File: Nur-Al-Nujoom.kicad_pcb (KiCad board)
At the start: 2 copper layers, 1 part, among them U1 STM32F030C8T6TR

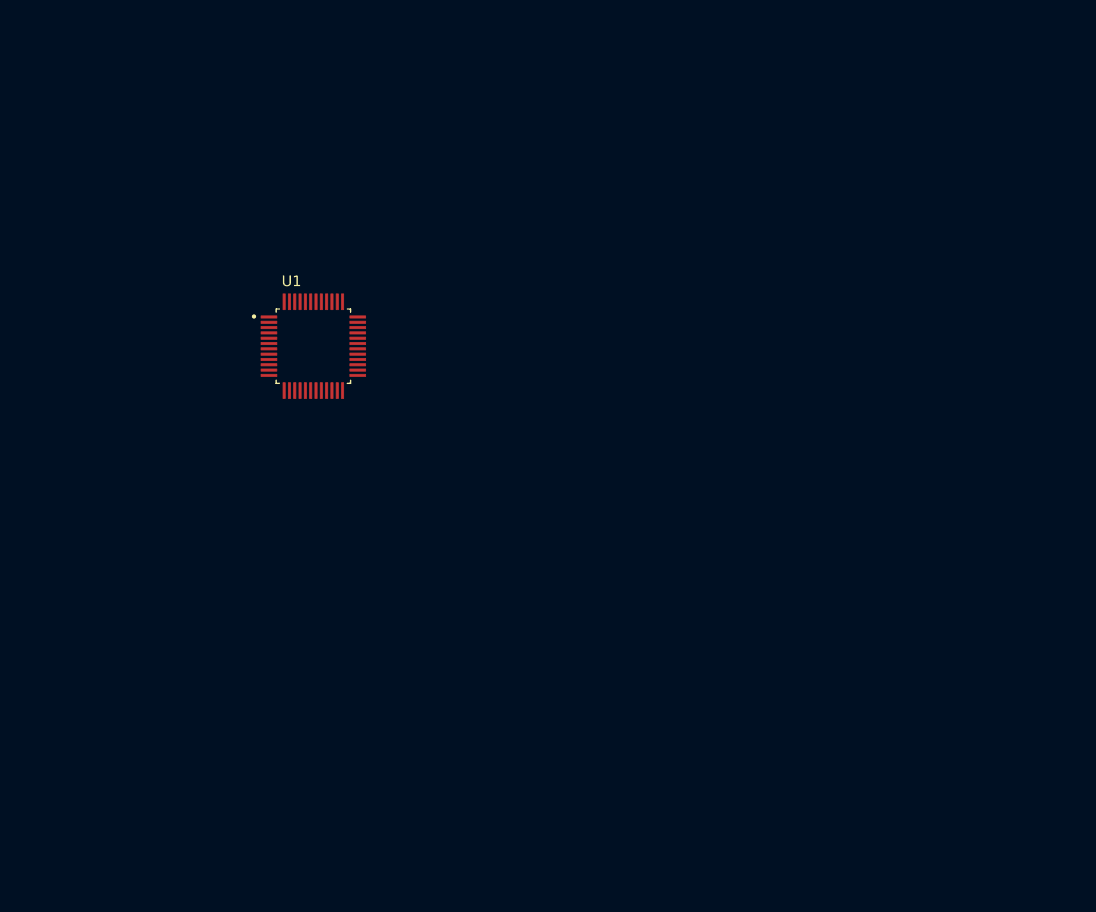
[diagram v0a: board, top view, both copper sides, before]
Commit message: updated Routing
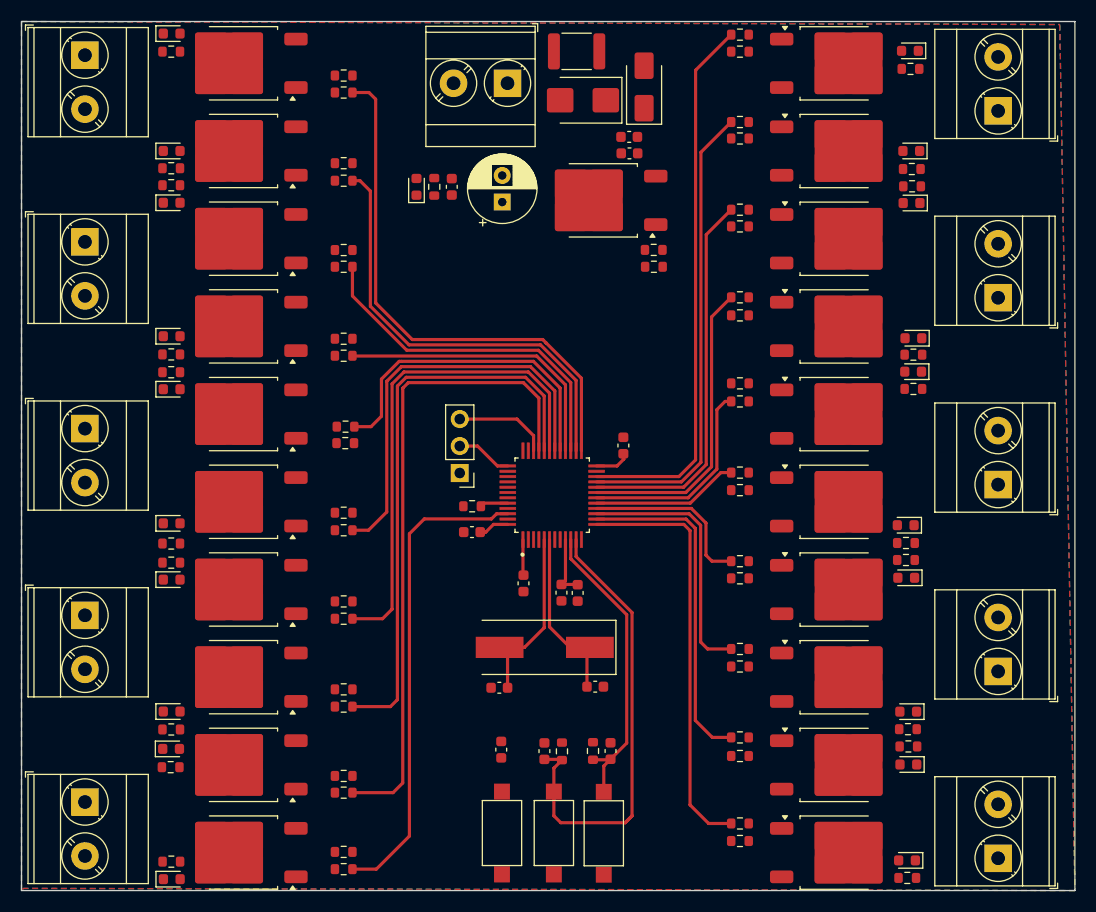
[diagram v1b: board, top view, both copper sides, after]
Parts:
- added C1: 10uF, Capacitor_SMD:C_0603_1608Metric, F.Cu at (172.7, 63.0)
- added C10: 100nF, Capacitor_SMD:C_0603_1608Metric, F.Cu at (160.7, 119.1)
- added C11: 20pF, Capacitor_SMD:C_0603_1608Metric, F.Cu at (169.5, 113.2)
- added C12: 20pF, Capacitor_SMD:C_0603_1608Metric, F.Cu at (160.5, 113.3)
- added C13: 100nF, Capacitor_SMD:C_0603_1608Metric, F.Cu at (170.9, 119.3)
- added C14: 100nF, Capacitor_SMD:C_0603_1608Metric, F.Cu at (164.7, 119.3)
- added C2: 100nF, Capacitor_SMD:C_0603_1608Metric, F.Cu at (172.7, 61.5)
- added C3: 100uF, Capacitor_THT:CP_Radial_D6.3mm_P2.50mm, F.Cu at (160.8, 67.6)
- added C4: 100nF, Capacitor_SMD:C_0603_1608Metric, F.Cu at (156.0, 66.2)
- added C5: 4.7uF, Capacitor_SMD:C_0603_1608Metric, F.Cu at (172.2, 90.5)
- added C6: 100nF, Capacitor_SMD:C_0603_1608Metric, F.Cu at (157.9, 98.7)
- added C7: 100nF, Capacitor_SMD:C_0603_1608Metric, F.Cu at (162.8, 103.5)
- added C8: 1uF, Capacitor_SMD:C_0603_1608Metric, F.Cu at (166.3, 104.3)
- added C9: 10nF, Capacitor_SMD:C_0603_1608Metric, F.Cu at (167.8, 104.4)
- added D1: SMBJ18CA, Diode_SMD:D_SMB, F.Cu at (168.3, 58.0)
- added D10: LED_Small, LED_SMD:LED_0603_1608Metric, F.Cu at (199.4, 83.5)
- added D11: LED_Small, LED_SMD:LED_0603_1608Metric, F.Cu at (199.2, 62.8)
- added D12: LED_Small, LED_SMD:LED_0603_1608Metric, F.Cu at (199.1, 53.4)
- added D13: LED_Small, LED_SMD:LED_0603_1608Metric, F.Cu at (199.4, 80.4)
- added D14: LED_Small, LED_SMD:LED_0603_1608Metric, F.Cu at (129.6, 115.5)
- added D15: LED_Small, LED_SMD:LED_0603_1608Metric, F.Cu at (129.6, 131.3)
- added D16: LED_Small, LED_SMD:LED_0603_1608Metric, F.Cu at (129.6, 103.1)
- added D17: LED_Small, LED_SMD:LED_0603_1608Metric, F.Cu at (129.6, 97.8)
- added D18: LED_Small, LED_SMD:LED_0603_1608Metric, F.Cu at (129.6, 119.1)
- added D19: LED_Small, LED_SMD:LED_0603_1608Metric, F.Cu at (129.6, 67.7)
- added D2: SS34, Diode_SMD:D_SMA, F.Cu at (174.1, 56.8)
- added D20: LED_Small, LED_SMD:LED_0603_1608Metric, F.Cu at (129.6, 85.2)
- added D21: LED_Small, LED_SMD:LED_0603_1608Metric, F.Cu at (129.6, 62.8)
- added D22: LED_Small, LED_SMD:LED_0603_1608Metric, F.Cu at (129.6, 51.7)
- added D23: LED_Small, LED_SMD:LED_0603_1608Metric, F.Cu at (129.6, 80.2)
- added D3: LED, LED_SMD:LED_0603_1608Metric, F.Cu at (152.7, 66.2)
- added D4: LED_Small, LED_SMD:LED_0603_1608Metric, F.Cu at (198.8, 129.6)
- added D5: LED_Small, LED_SMD:LED_0603_1608Metric, F.Cu at (199.0, 120.5)
- added D6: LED_Small, LED_SMD:LED_0603_1608Metric, F.Cu at (199.0, 115.5)
- added D7: LED_Small, LED_SMD:LED_0603_1608Metric, F.Cu at (198.8, 103.0)
- added D8: LED_Small, LED_SMD:LED_0603_1608Metric, F.Cu at (198.7, 98.0)
- added D9: LED_Small, LED_SMD:LED_0603_1608Metric, F.Cu at (199.3, 67.7)
- added J1: Main_12+, TerminalBlock_Phoenix:TerminalBlock_Phoenix_MKDS-3-2-5.08_1x02_P5.08mm_Horizontal, F.Cu at (161.2, 56.4)
- added J10: C1,2, TerminalBlock_Phoenix:TerminalBlock_Phoenix_MKDS-3-2-5.08_1x02_P5.08mm_Horizontal, F.Cu at (121.5, 88.9)
- added J11: C1,2, TerminalBlock_Phoenix:TerminalBlock_Phoenix_MKDS-3-2-5.08_1x02_P5.08mm_Horizontal, F.Cu at (121.5, 71.3)
- added J12: C1,2, TerminalBlock_Phoenix:TerminalBlock_Phoenix_MKDS-3-2-5.08_1x02_P5.08mm_Horizontal, F.Cu at (121.5, 53.8)
- added J2: SWD, Connector_PinHeader_2.54mm:PinHeader_1x03_P2.54mm_Vertical, F.Cu at (156.8, 93.1)
- added J3: C1,2, TerminalBlock_Phoenix:TerminalBlock_Phoenix_MKDS-3-2-5.08_1x02_P5.08mm_Horizontal, F.Cu at (207.4, 129.3)
- added J4: C1,2, TerminalBlock_Phoenix:TerminalBlock_Phoenix_MKDS-3-2-5.08_1x02_P5.08mm_Horizontal, F.Cu at (207.4, 111.8)
- added J5: C1,2, TerminalBlock_Phoenix:TerminalBlock_Phoenix_MKDS-3-2-5.08_1x02_P5.08mm_Horizontal, F.Cu at (207.4, 94.2)
- added J6: C1,2, TerminalBlock_Phoenix:TerminalBlock_Phoenix_MKDS-3-2-5.08_1x02_P5.08mm_Horizontal, F.Cu at (207.4, 76.6)
- added J7: C1,2, TerminalBlock_Phoenix:TerminalBlock_Phoenix_MKDS-3-2-5.08_1x02_P5.08mm_Horizontal, F.Cu at (207.4, 59.0)
- added J8: C1,2, TerminalBlock_Phoenix:TerminalBlock_Phoenix_MKDS-3-2-5.08_1x02_P5.08mm_Horizontal, F.Cu at (121.5, 124.1)
- added J9: C1,2, TerminalBlock_Phoenix:TerminalBlock_Phoenix_MKDS-3-2-5.08_1x02_P5.08mm_Horizontal, F.Cu at (121.5, 106.5)
- added Q1: MOT90N03D, Package_TO_SOT_SMD:TO-252-2, F.Cu at (192.1, 128.8)
- added Q10: MOT90N03D, Package_TO_SOT_SMD:TO-252-2, F.Cu at (192.1, 79.3)
- added Q11: MOT90N03D, Package_TO_SOT_SMD:TO-252-2, F.Cu at (136.3, 112.3)
- added Q12: MOT90N03D, Package_TO_SOT_SMD:TO-252-2, F.Cu at (136.3, 128.8)
- added Q13: MOT90N03D, Package_TO_SOT_SMD:TO-252-2, F.Cu at (136.3, 104.1)
- added Q14: MOT90N03D, Package_TO_SOT_SMD:TO-252-2, F.Cu at (136.3, 95.8)
- added Q15: MOT90N03D, Package_TO_SOT_SMD:TO-252-2, F.Cu at (136.3, 120.6)
- added Q16: MOT90N03D, Package_TO_SOT_SMD:TO-252-2, F.Cu at (136.3, 71.0)
- added Q17: MOT90N03D, Package_TO_SOT_SMD:TO-252-2, F.Cu at (136.3, 87.5)
- added Q18: MOT90N03D, Package_TO_SOT_SMD:TO-252-2, F.Cu at (136.3, 62.8)
- added Q19: MOT90N03D, Package_TO_SOT_SMD:TO-252-2, F.Cu at (136.3, 54.5)
- added Q2: MOT90N03D, Package_TO_SOT_SMD:TO-252-2, F.Cu at (192.1, 120.6)
- added Q20: MOT90N03D, Package_TO_SOT_SMD:TO-252-2, F.Cu at (136.3, 79.3)
- added Q3: MOT90N03D, Package_TO_SOT_SMD:TO-252-2, F.Cu at (192.1, 112.3)
- added Q4: MOT90N03D, Package_TO_SOT_SMD:TO-252-2, F.Cu at (192.1, 104.1)
- added Q5: MOT90N03D, Package_TO_SOT_SMD:TO-252-2, F.Cu at (192.1, 95.8)
- added Q6: MOT90N03D, Package_TO_SOT_SMD:TO-252-2, F.Cu at (192.1, 71.0)
- added Q7: MOT90N03D, Package_TO_SOT_SMD:TO-252-2, F.Cu at (192.1, 87.5)
- added Q8: MOT90N03D, Package_TO_SOT_SMD:TO-252-2, F.Cu at (192.1, 62.8)
- added Q9: MOT90N03D, Package_TO_SOT_SMD:TO-252-2, F.Cu at (192.1, 54.5)
- added R1: 240R, Resistor_SMD:R_0603_1608Metric, F.Cu at (154.3, 66.2)
- added R10: 2.2k, Resistor_SMD:R_0603_1608Metric, F.Cu at (199.0, 118.8)
- added R11: 240R, Resistor_SMD:R_0603_1608Metric, F.Cu at (183.1, 109.7)
- added R12: 10K, Resistor_SMD:R_0603_1608Metric, F.Cu at (183.1, 111.3)
- added R13: 2.2k, Resistor_SMD:R_0603_1608Metric, F.Cu at (198.9, 117.2)
- added R14: 240R, Resistor_SMD:R_0603_1608Metric, F.Cu at (183.1, 101.4)
- added R15: 10K, Resistor_SMD:R_0603_1608Metric, F.Cu at (183.1, 103.0)
- added R16: 2.2k, Resistor_SMD:R_0603_1608Metric, F.Cu at (198.8, 101.3)
- added R17: 240R, Resistor_SMD:R_0603_1608Metric, F.Cu at (183.1, 93.0)
- added R18: 10K, Resistor_SMD:R_0603_1608Metric, F.Cu at (183.1, 94.7)
- added R19: 2.2k, Resistor_SMD:R_0603_1608Metric, F.Cu at (198.8, 99.7)
- added R2: 10K, Resistor_SMD:R_0603_1608Metric, F.Cu at (157.9, 96.2)
- added R20: 240R, Resistor_SMD:R_0603_1608Metric, F.Cu at (183.1, 68.3)
- added R21: 240R, Resistor_SMD:R_0603_1608Metric, F.Cu at (183.1, 86.3)
- added R22: 240R, Resistor_SMD:R_0603_1608Metric, F.Cu at (183.1, 60.0)
- added R23: 240R, Resistor_SMD:R_0603_1608Metric, F.Cu at (183.1, 51.8)
- added R24: 240R, Resistor_SMD:R_0603_1608Metric, F.Cu at (183.1, 76.5)
- added R25: 10K, Resistor_SMD:R_0603_1608Metric, F.Cu at (183.1, 69.9)
- added R26: 10K, Resistor_SMD:R_0603_1608Metric, F.Cu at (183.1, 84.7)
- added R27: 10K, Resistor_SMD:R_0603_1608Metric, F.Cu at (183.1, 61.6)
- added R28: 10K, Resistor_SMD:R_0603_1608Metric, F.Cu at (183.1, 53.4)
- added R29: 10K, Resistor_SMD:R_0603_1608Metric, F.Cu at (183.1, 78.2)
- added R3: 10K, Resistor_SMD:R_0603_1608Metric, F.Cu at (169.3, 119.3)
- added R30: 2.2k, Resistor_SMD:R_0603_1608Metric, F.Cu at (199.3, 66.1)
- added R31: 2.2k, Resistor_SMD:R_0603_1608Metric, F.Cu at (199.4, 85.2)
- added R32: 2.2k, Resistor_SMD:R_0603_1608Metric, F.Cu at (199.3, 64.5)
- added R33: 2.2k, Resistor_SMD:R_0603_1608Metric, F.Cu at (199.2, 55.0)
- added R34: 2.2k, Resistor_SMD:R_0603_1608Metric, F.Cu at (199.4, 82.0)
- added R35: 240R, Resistor_SMD:R_0603_1608Metric, F.Cu at (145.8, 115.1)
- added R36: 240R, Resistor_SMD:R_0603_1608Metric, F.Cu at (145.8, 130.4)
- added R37: 240R, Resistor_SMD:R_0603_1608Metric, F.Cu at (145.8, 106.8)
- added R38: 240R, Resistor_SMD:R_0603_1608Metric, F.Cu at (145.8, 98.5)
- added R39: 240R, Resistor_SMD:R_0603_1608Metric, F.Cu at (145.8, 123.2)
- added R4: 10K, Resistor_SMD:R_0603_1608Metric, F.Cu at (166.4, 119.3)
- added R40: 10K, Resistor_SMD:R_0603_1608Metric, F.Cu at (145.8, 113.5)
- added R41: 10K, Resistor_SMD:R_0603_1608Metric, F.Cu at (145.8, 128.8)
- added R42: 10K, Resistor_SMD:R_0603_1608Metric, F.Cu at (145.8, 105.2)
- added R43: 10K, Resistor_SMD:R_0603_1608Metric, F.Cu at (145.8, 96.8)
- added R44: 10K, Resistor_SMD:R_0603_1608Metric, F.Cu at (145.8, 121.6)
- added R45: 2.2k, Resistor_SMD:R_0603_1608Metric, F.Cu at (129.6, 117.2)
- added R46: 2.2k, Resistor_SMD:R_0603_1608Metric, F.Cu at (129.6, 129.7)
- added R47: 2.2k, Resistor_SMD:R_0603_1608Metric, F.Cu at (129.6, 101.5)
- added R48: 2.2k, Resistor_SMD:R_0603_1608Metric, F.Cu at (129.6, 99.7)
- added R49: 2.2k, Resistor_SMD:R_0603_1608Metric, F.Cu at (129.5, 120.8)
- added R5: 240R, Resistor_SMD:R_0603_1608Metric, F.Cu at (183.1, 126.1)
- added R50: 240R, Resistor_SMD:R_0603_1608Metric, F.Cu at (145.8, 73.7)
- added R51: 240R, Resistor_SMD:R_0603_1608Metric, F.Cu at (146.0, 88.7)
- added R52: 240R, Resistor_SMD:R_0603_1608Metric, F.Cu at (145.8, 65.6)
- added R53: 240R, Resistor_SMD:R_0603_1608Metric, F.Cu at (145.8, 57.3)
- added R54: 240R, Resistor_SMD:R_0603_1608Metric, F.Cu at (145.8, 82.0)
- added R55: 10K, Resistor_SMD:R_0603_1608Metric, F.Cu at (145.8, 72.1)
- added R56: 10K, Resistor_SMD:R_0603_1608Metric, F.Cu at (146.0, 90.3)
- added R57: 10K, Resistor_SMD:R_0603_1608Metric, F.Cu at (145.8, 63.9)
- added R58: 10K, Resistor_SMD:R_0603_1608Metric, F.Cu at (145.8, 55.7)
- added R59: 10K, Resistor_SMD:R_0603_1608Metric, F.Cu at (145.8, 80.5)
- added R6: 10K, Resistor_SMD:R_0603_1608Metric, F.Cu at (183.1, 127.7)
- added R60: 2.2k, Resistor_SMD:R_0603_1608Metric, F.Cu at (129.6, 66.0)
- added R61: 2.2k, Resistor_SMD:R_0603_1608Metric, F.Cu at (129.6, 83.6)
- added R62: 2.2k, Resistor_SMD:R_0603_1608Metric, F.Cu at (129.6, 64.4)
- added R63: 2.2k, Resistor_SMD:R_0603_1608Metric, F.Cu at (129.6, 53.4)
- added R64: 2.2k, Resistor_SMD:R_0603_1608Metric, F.Cu at (129.6, 81.9)
- added R65: 240R, Resistor_SMD:R_0603_1608Metric, F.Cu at (175.0, 72.1)
- added R66: 402R, Resistor_SMD:R_0603_1608Metric, F.Cu at (175.0, 73.7)
- added R7: 2.2k, Resistor_SMD:R_0603_1608Metric, F.Cu at (198.9, 131.2)
- added R8: 240R, Resistor_SMD:R_0603_1608Metric, F.Cu at (183.1, 118.0)
- added R9: 10K, Resistor_SMD:R_0603_1608Metric, F.Cu at (183.1, 119.7)
- added SW1: SW_SPST, Button_Switch_SMD:SW_SPST_CK_RS282G05A3, F.Cu at (160.7, 127.0)
- added SW2: SW_SPST, Button_Switch_SMD:SW_SPST_CK_RS282G05A3, F.Cu at (170.3, 127.0)
- added SW3: SW_SPST, Button_Switch_SMD:SW_SPST_CK_RS282G05A3, F.Cu at (165.6, 127.0)
- added TH1: Thermistor_PTC, Fuse:Fuse_1812_4532Metric, F.Cu at (167.8, 53.4)
- added U3: LM317_TO-252, Package_TO_SOT_SMD:TO-252-2, F.Cu at (170.2, 67.4)
- added Y1: 8MHZ, Crystal:Crystal_SMD_HC49-SD, F.Cu at (164.8, 109.5)
- moved U1 26.5 mm to (165.4, 95.2), turned to 90 degrees
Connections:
- U1 pad 1: /MCU/VDD -> /MCU/VCC_3v3
- U1 pad 12: /MCU/PA2 -> unconnected-(U1-PA2-Pad12)
- U1 pad 2: /MCU/PC13 -> unconnected-(U1-PC13-Pad2)
- U1 pad 23: /MCU/VSS -> GND
- U1 pad 24: /MCU/VDD__1 -> /MCU/VCC_3v3
- U1 pad 3: /MCU/PC14-OSC32_IN -> unconnected-(U1-PC14-OSC32_IN-Pad3)
- U1 pad 35: /MCU/PF6 -> unconnected-(U1-PF6-Pad35)
- U1 pad 36: /MCU/PF7 -> unconnected-(U1-PF7-Pad36)
- U1 pad 38: /MCU/PA15 -> unconnected-(U1-PA15-Pad38)
- U1 pad 39: /MCU/PB3 -> unconnected-(U1-PB3-Pad39)
- U1 pad 4: /MCU/PC15-OSC32_OUT -> unconnected-(U1-PC15-OSC32_OUT-Pad4)
- U1 pad 40: /MCU/PB4 -> unconnected-(U1-PB4-Pad40)
- U1 pad 41: /MCU/PB5 -> unconnected-(U1-PB5-Pad41)
- U1 pad 42: /MCU/PB6 -> unconnected-(U1-PB6-Pad42)
- U1 pad 43: /MCU/PB7 -> unconnected-(U1-PB7-Pad43)
- U1 pad 45: /MCU/PB8 -> unconnected-(U1-PB8-Pad45)
- U1 pad 47: /MCU/VSS__1 -> GND
- U1 pad 48: /MCU/VDD__2 -> /MCU/VCC_3v3
- U1 pad 8: /MCU/VSSA -> GND
- U1 pad 9: /MCU/VDDA -> /MCU/VCC_3v3
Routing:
- net /MCU/PA12: track 0.00 -> 60.9 mm
- net /MCU/PA11: track 0.00 -> 54.1 mm
- net /MCU/PB11: track 0.00 -> 51.4 mm
- net /MCU/PB12: track 0.00 -> 50.8 mm
- net /MCU/PA10: track 0.00 -> 46.8 mm
- net /MCU/PB9: track 0.00 -> 45.1 mm
- net /MCU/PA1: track 0.00 -> 44.2 mm
- net /MCU/PB10: track 0.00 -> 43.8 mm
- net /MCU/PB13: track 0.00 -> 41.8 mm
- net /MCU/PA3: track 0.00 -> 39.5 mm
- net /MCU/PA9: track 0.00 -> 39.2 mm
- net /MCU/PB2: track 0.00 -> 36.2 mm
- net /MCU/PB14: track 0.00 -> 33.1 mm
- net /MCU/PA4: track 0.00 -> 31.8 mm
- net /MCU/PA8: track 0.00 -> 30.9 mm
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- added copper zone on B.Cu, net GND
- added copper zone on F.Cu, net GND
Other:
- board outline added: 99.2 x 81.8 mm
